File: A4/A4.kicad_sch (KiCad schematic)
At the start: 4 parts, among them J1 Power, J2 Digital/PWM, J3 Analog, J4 Digital/PWM

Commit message: PCB 10%
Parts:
- added BZ1: Buzzer, symbol Device:Buzzer
- added D1: LED, symbol Device:LED
- added J10: LDR, symbol Connector:Conn_01x03_Pin
- added J11: GAS, symbol Connector:Conn_01x04_Pin
- added J5: Servo, symbol Connector:Conn_01x03_Pin
- added J6: Ultrasonic sensor, symbol Connector:Conn_01x04_Pin
- added J7: DHT11, symbol Connector:Conn_01x03_Pin
- added J8: TEST_PIN, symbol Connector:Conn_01x02_Pin
- added J9: 0.96" Oled, symbol Connector:Conn_01x04_Pin
- added POWER_PLUG: 3V3/5V, symbol Connector:Conn_01x03_Pin
- added R1: 330, symbol Device:R_US
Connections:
- net *10: now also J6.3 (Pin_3)
- net *9: now also J10.1 (Pin_1), J11.2 (Pin_2), J5.1 (Pin_1), J6.2 (Pin_2), J7.2 (Pin_2)
- net +3V3: now also POWER_PLUG.3 (Pin_3)
- net +5V: now also BZ1.1 (+), POWER_PLUG.1 (Pin_1)
- net A0: now also J11.1 (Pin_1)
- net GND: now also J10.2 (Pin_2), J11.3 (Pin_3), J5.3 (Pin_3), J6.1 (Pin_1), J7.1 (Pin_1), J8.1 (Pin_1), J9.4 (Pin_4)
- net SCL/A5: now also J9.2 (Pin_2)
- net SDA/A4: now also J9.1 (Pin_1)
- new net: BZ1.2 (-), J8.2 (Pin_2)
- new net: D1.2 (A), R1.1
- new net VDD: J10.3 (Pin_3), J11.4 (Pin_4), J5.2 (Pin_2), J6.4 (Pin_4), J7.3 (Pin_3), J9.3 (Pin_3), POWER_PLUG.2 (Pin_2)
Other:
- note added: "Attach VDD for powering Attach GND for grounding Attach Ana_in for Analog input Attach Dig_in for Digital output"
- note added: "EXTRAAS"
- note added: "Restricted zone"
- note added: "Sensors info:"
- title: (none) -> ISA COMMUNITY 26'

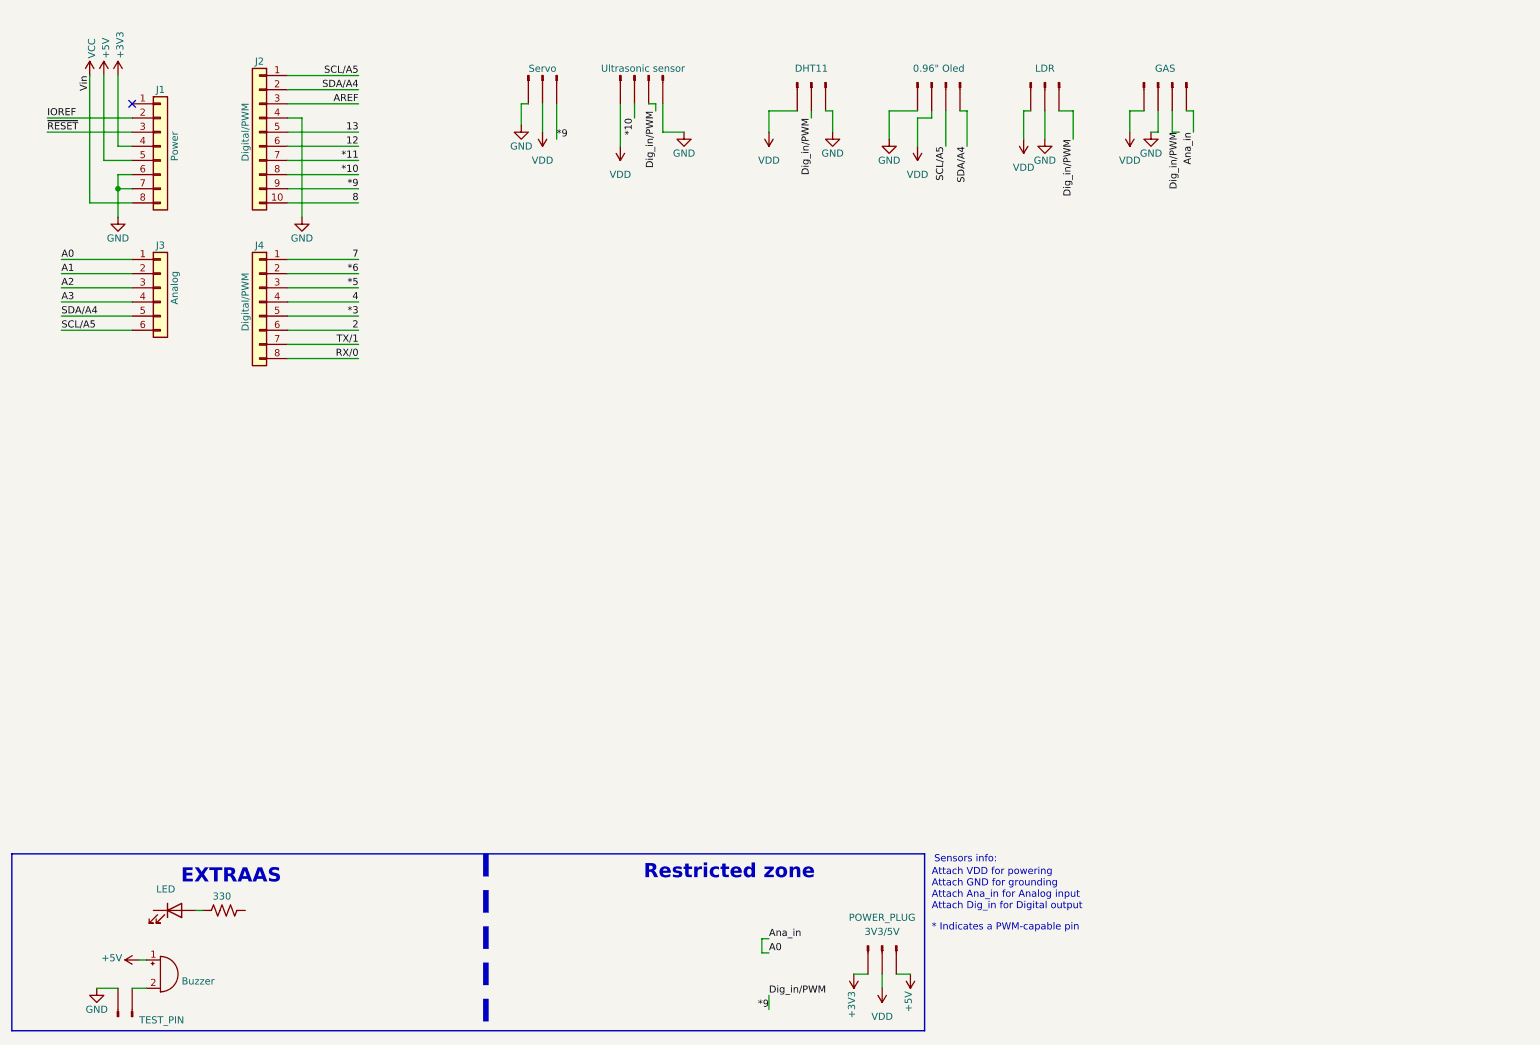
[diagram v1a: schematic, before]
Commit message: Pcb 28%
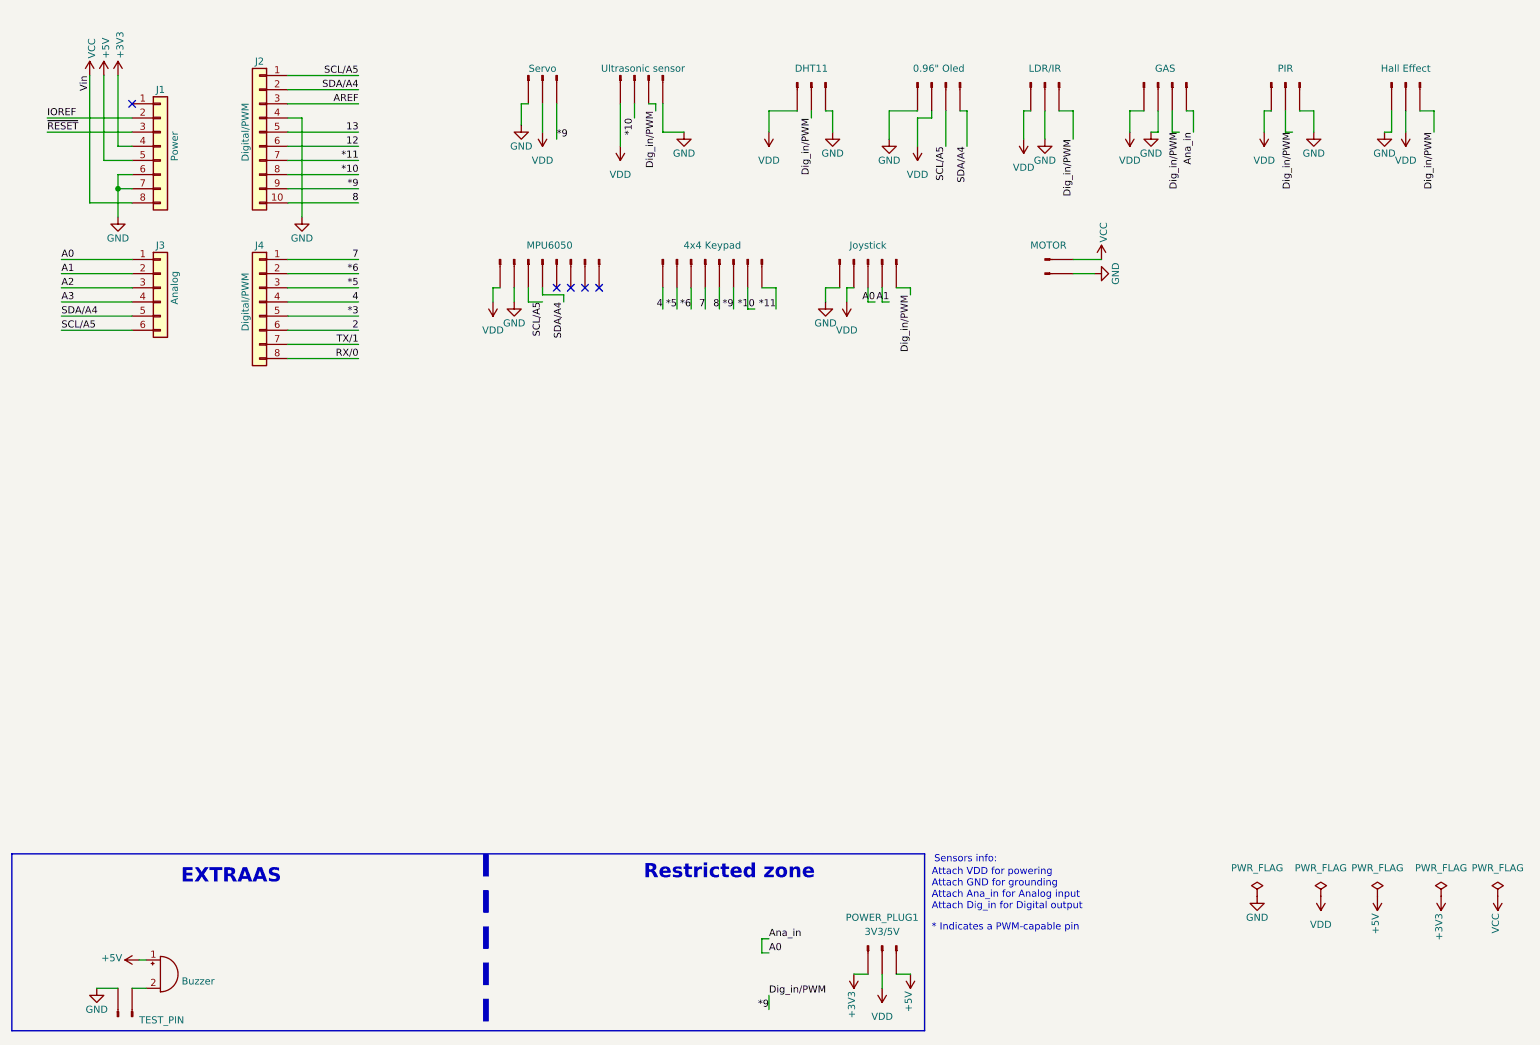
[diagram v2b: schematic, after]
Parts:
- removed D1: LED, symbol Device:LED
- removed R1: 330, symbol Device:R_US
- added J12: PIR, Connector_PinSocket_2.54mm:PinSocket_1x03_P2.54mm_Vertical, symbol Connector:Conn_01x03_Pin
- added J13: Hall Effect, Connector_PinSocket_2.54mm:PinSocket_1x03_P2.54mm_Vertical, symbol Connector:Conn_01x03_Pin
- added J14: MPU6050, Connector_PinSocket_2.54mm:PinSocket_1x08_P2.54mm_Vertical, symbol Connector:Conn_01x08_Pin
- added J15: 4x4 Keypad, Connector_PinSocket_2.54mm:PinSocket_1x08_P2.54mm_Vertical, symbol Connector:Conn_01x08_Pin
- added J16: Joystick, Connector_PinSocket_2.54mm:PinSocket_1x04_P2.54mm_Vertical, symbol Connector:Conn_01x05_Pin
- added J17: MOTOR, symbol Connector:Conn_01x02_Pin
- J10: value LDR -> LDR/IR; footprint (none) -> Connector_PinSocket_2.54mm:PinSocket_1x03_P2.54mm_Vertical
- J11, J6, J9: footprint (none) -> Connector_PinSocket_2.54mm:PinSocket_1x04_P2.54mm_Vertical
- J5, J7: footprint (none) -> Connector_PinSocket_2.54mm:PinSocket_1x03_P2.54mm_Vertical
- J8: footprint (none) -> Connector_PinSocket_2.54mm:PinSocket_1x02_P2.54mm_Vertical
- POWER_PLUG1: renamed from POWER_PLUG; footprint (none) -> Connector_PinSocket_2.54mm:PinSocket_1x03_P2.54mm_Vertical
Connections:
- net *10: now also J15.2 (Pin_2)
- net *11: now also J15.1 (Pin_1)
- net *5: now also J15.7 (Pin_7)
- net *6: now also J15.6 (Pin_6)
- net *9: now also J12.2 (Pin_2), J13.1 (Pin_1), J15.3 (Pin_3), J16.1 (Pin_1)
- net 4: now also J15.8 (Pin_8)
- net 7: now also J15.5 (Pin_5)
- net 8: now also J15.4 (Pin_4)
- net A0: now also J16.3 (Pin_3)
- net A1: now also J16.2 (Pin_2)
- net GND: now also J12.1 (Pin_1), J13.3 (Pin_3), J14.7 (Pin_7), J16.5 (Pin_5), J17.2 (Pin_2)
- net SCL/A5: now also J14.6 (Pin_6)
- net SDA/A4: now also J14.5 (Pin_5)
- net VCC: now also J17.1 (Pin_1)
- net VDD: now also J12.3 (Pin_3), J13.2 (Pin_2), J14.8 (Pin_8), J16.4 (Pin_4)
- no-connect marks 1 -> 5

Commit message: PCB 45%
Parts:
- removed J1: Power, Connector_PinSocket_2.54mm:PinSocket_1x08_P2.54mm_Vertical, symbol Connector_Generic:Conn_01x08
- removed J2: Digital/PWM, Connector_PinSocket_2.54mm:PinSocket_1x10_P2.54mm_Vertical, symbol Connector_Generic:Conn_01x10
- removed J3: Analog, Connector_PinSocket_2.54mm:PinSocket_1x06_P2.54mm_Vertical, symbol Connector_Generic:Conn_01x06
- removed J4: Digital/PWM, Connector_PinSocket_2.54mm:PinSocket_1x08_P2.54mm_Vertical, symbol Connector_Generic:Conn_01x08
- added A1: Arduino_Nano_v2.x, Module:Arduino_Nano, symbol MCU_Module:Arduino_Nano_v2.x
- added J1: RFID, Connector_PinHeader_2.54mm:PinHeader_1x08_P2.54mm_Vertical, symbol Connector:Conn_01x08_Pin
- added J2: I2C 16X2, Connector_PinHeader_2.54mm:PinHeader_1x04_P2.54mm_Vertical, symbol Connector:Conn_01x04_Pin
- BZ1, J17: footprint (none) -> TerminalBlock_Phoenix:TerminalBlock_Phoenix_MKDS-1,5-2-5.08_1x02_P5.08mm_Horizontal
- J16: footprint Connector_PinSocket_2.54mm:PinSocket_1x04_P2.54mm_Vertical -> Connector_PinSocket_2.54mm:PinSocket_1x05_P2.54mm_Vertical
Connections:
- net *10: now also A1.13 (D10), J1.1 (Pin_1)
- net *11: now also A1.14 (D11), J1.3 (Pin_3)
- net *3: now also A1.6 (D3)
- net *5: now also A1.8 (D5)
- net *6: now also A1.9 (D6)
- net *9: now also A1.12 (D9), J1.7 (Pin_7)
- net +3V3: now also A1.17 (3V3), J1.8 (Pin_8)
- net +5V: now also A1.27 (+5V), J2.3 (Pin_3)
- net 12: now also A1.15 (D12), J1.4 (Pin_4)
- net 13: now also A1.16 (D13), J1.2 (Pin_2)
- net 2: now also A1.5 (D2)
- net 4: now also A1.7 (D4)
- net 7: now also A1.10 (D7)
- net 8: now also A1.11 (D8)
- net A0: now also A1.19 (A0)
- net A1: now also A1.20 (A1)
- net A2: now also A1.21 (A2)
- net A3: now also A1.22 (A3)
- net GND: now also A1.29 (GND), A1.4 (GND), J1.6 (Pin_6), J2.4 (Pin_4)
- net RX/0: now also A1.2 (D0/RX)
- net SCL/A5: now also A1.24 (A5), J2.1 (Pin_1)
- net SDA/A4: now also A1.23 (A4), J2.2 (Pin_2)
- net TX/1: now also A1.1 (D1/TX)
- net VCC: now also A1.30 (VIN)
- no-connect marks 5 -> 10

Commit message: PCB 66%
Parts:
- added J18, J19, J20, J21, J22, J23, J24, J25, J26, J27, J4: Conn_01x01_Pin, Connector_PinHeader_2.54mm:PinHeader_1x01_P2.54mm_Vertical, symbol Connector:Conn_01x01_Pin
- added J3: TX/RX, Connector_PinHeader_2.54mm:PinHeader_1x04_P2.54mm_Vertical, symbol Connector:Conn_01x04_Pin
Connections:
- net *10: now also J1.4 (Pin_4); no longer J1.1 (Pin_1)
- net *11: now also J10.1 (Pin_1), J11.2 (Pin_2), J12.2 (Pin_2), J13.1 (Pin_1), J16.1 (Pin_1), J5.1 (Pin_1), J6.2 (Pin_2), J7.2 (Pin_2)
- net *9: no longer J10.1 (Pin_1), J11.2 (Pin_2), J12.2 (Pin_2), J13.1 (Pin_1), J16.1 (Pin_1), J5.1 (Pin_1), J6.2 (Pin_2), J7.2 (Pin_2)
- net +5V: now also J25.1 (Pin_1), J26.1 (Pin_1)
- net 12: now also J1.2 (Pin_2); no longer J1.4 (Pin_4)
- net 13: now also J1.1 (Pin_1); no longer J1.2 (Pin_2)
- net A0: now also J16.2 (Pin_2); no longer J16.3 (Pin_3)
- net A1: now also J16.3 (Pin_3); no longer J16.2 (Pin_2)
- net GND: now also J18.1 (Pin_1), J19.1 (Pin_1), J20.1 (Pin_1), J27.1 (Pin_1), J3.3 (Pin_3), J4.1 (Pin_1)
- net RX/0: now also J3.2 (Pin_2)
- net TX/1: now also J3.1 (Pin_1)
- net VDD: now also J21.1 (Pin_1), J22.1 (Pin_1), J23.1 (Pin_1), J24.1 (Pin_1), J3.4 (Pin_4)
